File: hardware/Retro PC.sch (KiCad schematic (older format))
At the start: 0 parts

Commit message: Working on Schematic
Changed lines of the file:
@@
 $Descr A3 16535 11693
 encoding utf-8
-Sheet 1 5
+Sheet 1 6
 Title "Retro PC"
 Date "2019-10-08"
@@
 Wire Wire Line
 	10250 5450 10250 6500
+$Sheet
+S 8300 9600 1350 1250
+U 5DADBF97
+F0 "LCD" 50
+F1 "LCD.sch" 50
+$EndSheet
 $EndSCHEMATC

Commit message: Working on layout
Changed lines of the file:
@@
 Wire Wire Line
 	6500 4900 8000 4900
-$Sheet
-S 8250 6250 1600 1550
-U 5EB09E21
-F0 "Processor" 50
-F1 "Processor.sch" 50
-F2 "~RESET" I L 8250 6450 50
-F3 "PA[0..7]" O R 9850 7400 50
-F4 "CB[1..2]" I R 9850 7700 50
-F5 "PB[0..7]" I R 9850 7500 50
-F6 "TxD" O R 9850 6400 50
-F7 "RxD" I R 9850 6500 50
-F8 "RTS" O R 9850 6600 50
-F9 "CTS" I R 9850 6700 50
-F10 "ModemReady" I R 9850 6800 50
-F11 "ACIAReady" O R 9850 7300 50
-F12 "RDY" O L 8250 7500 50
-F13 "~NMI" I L 8250 7400 50
-F14 "SYNC" O L 8250 7600 50
-F15 "VPB" O L 8250 7700 50
-F16 "BE" I L 8250 7300 50
-F17 "~IRQ" I L 8250 7200 50
-$EndSheet
 Wire Wire Line
 	8250 6450 8000 6450
@@
 F4 "PA[0..7]" O R 9650 8600 50
 F5 "ACIAReady" I R 9650 8700 50
-F6 "VPB" I L 8250 9250 50
-F7 "SYNC" I L 8250 9150 50
-F8 "RDY" O L 8250 9050 50
-F9 "~NMI" O L 8250 8950 50
-F10 "BE" O L 8250 8850 50
-F11 "~IRQ" O L 8250 8750 50
+F6 "~NMI" O L 8250 8950 50
+F7 "~IRQ" O L 8250 8750 50
+F8 "R~W" I R 9650 9150 50
+F9 "A[15..0]" I R 9650 8950 50
+F10 "D[7..0]" B R 9650 9050 50
+F11 "1MHz" I R 9650 9250 50
+F12 "~RESET" O L 8250 8350 50
 $EndSheet
 Wire Bus Line
@@
 Wire Wire Line
 	9650 8700 10500 8700
-Wire Wire Line
-	10500 8700 10500 7300
-Wire Wire Line
-	10500 7300 9850 7300
 Text Notes 3550 2350 0    100  ~ 0
 VIA 1
@@
 24K
 Wire Wire Line
-	8250 9250 7550 9250
-Wire Wire Line
-	7550 9250 7550 7700
-Wire Wire Line
-	7550 7700 8250 7700
-Wire Wire Line
-	8250 9150 7650 9150
-Wire Wire Line
-	7650 9150 7650 7600
-Wire Wire Line
-	7650 7600 8250 7600
-Wire Wire Line
-	8250 7500 7750 7500
-Wire Wire Line
-	7750 7500 7750 9050
-Wire Wire Line
-	7750 9050 8250 9050
-Wire Wire Line
-	8250 8950 7850 8950
-Wire Wire Line
-	7850 8950 7850 7400
-Wire Wire Line
-	7850 7400 8250 7400
-Wire Wire Line
-	8250 7300 7950 7300
-Wire Wire Line
-	7950 7300 7950 8850
-Wire Wire Line
-	7950 8850 8250 8850
-Wire Wire Line
-	8250 8750 8050 8750
-Wire Wire Line
-	8050 8750 8050 7200
-Wire Wire Line
-	8050 7200 8250 7200
+	8250 8950 7800 8950
+Wire Wire Line
+	7800 8950 7800 7400
+Wire Wire Line
+	7800 7400 8250 7400
+Wire Wire Line
+	8250 8750 7900 8750
+Wire Wire Line
+	7900 7200 8250 7200
 Wire Wire Line
 	10250 5450 10250 6500
@@
 F1 "LCD.sch" 50
 $EndSheet
+$Sheet
+S 8250 6250 1600 1550
+U 5EB09E21
+F0 "Processor" 50
+F1 "Processor.sch" 50
+F2 "~RESET" I L 8250 6450 50
+F3 "PA[0..7]" O R 9850 7400 50
+F4 "CB[1..2]" I R 9850 7700 50
+F5 "PB[0..7]" I R 9850 7500 50
+F6 "TxD" O R 9850 6400 50
+F7 "RxD" I R 9850 6500 50
+F8 "RTS" O R 9850 6600 50
+F9 "CTS" I R 9850 6700 50
+F10 "ModemReady" I R 9850 6800 50
+F11 "ACIAReady" O R 9850 7600 50
+F12 "~NMI" I L 8250 7400 50
+F13 "~IRQ" I L 8250 7200 50
+F14 "LCD[0..7]" I L 8250 6700 50
+F15 "R~W" O R 9850 7150 50
+F16 "A[15..0]" O R 9850 6950 50
+F17 "D[7..0]" B R 9850 7050 50
+F18 "1MHz" O R 9850 7250 50
+$EndSheet
+Wire Bus Line
+	9850 6950 10900 6950
+Wire Bus Line
+	10900 6950 10900 8950
+Wire Bus Line
+	10900 8950 9650 8950
+Wire Bus Line
+	10800 7050 10800 9050
+Wire Bus Line
+	10800 9050 9650 9050
+Wire Bus Line
+	9850 7050 10800 7050
+Wire Wire Line
+	9650 9150 10700 9150
+Wire Wire Line
+	10700 7150 9850 7150
+Wire Wire Line
+	10700 9150 10700 7150
+Wire Wire Line
+	10500 8700 10500 7600
+Wire Wire Line
+	10500 7600 9850 7600
+Wire Wire Line
+	9850 7250 10600 7250
+Wire Wire Line
+	10600 7250 10600 9250
+Wire Wire Line
+	10600 9250 9650 9250
+Wire Wire Line
+	7900 8750 7900 7200
+Connection ~ 8000 6450
+Wire Wire Line
+	8250 8350 8000 8350
+Wire Wire Line
+	8000 6450 8000 8350
 $EndSCHEMATC

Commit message: Working on layout
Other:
- note added: "VIA 2"
- note removed: "VIA 2 (Not available)"
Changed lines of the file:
@@
 VIA 1
 Text Notes 3550 2600 0    100  ~ 0
-VIA 2 (Not available)
+VIA 2
 Text Notes 900  2600 0    100  ~ 0
 $8400 - $87FF

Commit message: Working on layout
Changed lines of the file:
@@
 F2 "~RESET" O R 6500 4900 50
-$EndSheet
-$Sheet
-S 8200 4700 1650 1250
-U 5E9064F2
-F0 "USB" 50
-F1 "USB.sch" 50
-F2 "~RESET" I L 8200 4900 50
-F3 "TxD" I R 9850 5450 50
-F4 "RxD" I R 9850 5550 50
-F5 "CTS" I R 9850 5650 50
-F6 "RTS" O R 9850 5750 50
-F7 "ModemReady" O R 9850 5850 50
 $EndSheet
 Wire Bus Line
@@
 F3 "PB[0..7]" O R 9650 8500 50
 F4 "PA[0..7]" O R 9650 8600 50
-F5 "ACIAReady" I R 9650 8700 50
-F6 "~NMI" O L 8250 8950 50
-F7 "~IRQ" O L 8250 8750 50
-F8 "R~W" I R 9650 9150 50
-F9 "A[15..0]" I R 9650 8950 50
-F10 "D[7..0]" B R 9650 9050 50
-F11 "1MHz" I R 9650 9250 50
-F12 "~RESET" O L 8250 8350 50
+F5 "~NMI" O L 8250 8950 50
+F6 "~IRQ" O L 8250 8750 50
+F7 "R~W" I R 9650 9150 50
+F8 "A[15..0]" I R 9650 8950 50
+F9 "D[7..0]" B R 9650 9050 50
+F10 "~RESET" O L 8250 8350 50
+F11 "Clock" I R 9650 9250 50
 $EndSheet
 Wire Bus Line
 	9650 8500 10250 8500
 Wire Bus Line
-	10250 8500 10250 7500
+	10250 8500 10250 7600
 Wire Bus Line
 	9650 8600 10350 8600
 Wire Bus Line
-	10350 8600 10350 7400
+	10350 8600 10350 7500
 Text Notes 900  1850 0    100  ~ 0
 $0000 - $FFFF\n
@@
 Wire Notes Line width 18 style solid
 	750  1150 750  3700
-Wire Bus Line
-	9850 7400 10350 7400
-Wire Bus Line
-	9850 7500 10250 7500
 Wire Wire Line
 	9850 5450 10250 5450
@@
 	9850 5650 10150 5650
 Wire Wire Line
-	10150 5650 10150 6600
+	10150 5650 10150 6550
 Wire Wire Line
-	10150 6600 9850 6600
-Wire Wire Line
-	9850 6700 10100 6700
-Wire Wire Line
-	10100 6700 10100 5750
+	10150 6550 9850 6550
 Wire Wire Line
 	10100 5750 9850 5750
@@
 	9850 5850 10050 5850
 Wire Wire Line
-	10050 5850 10050 6800
+	10050 5850 10050 6750
 Wire Wire Line
-	10050 6800 9850 6800
+	10050 6750 9850 6750
 Wire Wire Line
-	9850 6400 10200 6400
+	9850 6350 10200 6350
 Wire Wire Line
-	10200 6400 10200 5550
+	10200 6350 10200 5550
 Wire Wire Line
-	9850 6500 10250 6500
-Wire Wire Line
-	9650 8700 10500 8700
+	9850 6450 10250 6450
 Text Notes 3550 2350 0    100  ~ 0
 VIA 1
@@
 	8250 8950 7800 8950
 Wire Wire Line
-	7800 8950 7800 7400
-Wire Wire Line
-	7800 7400 8250 7400
-Wire Wire Line
 	8250 8750 7900 8750
 Wire Wire Line
-	7900 7200 8250 7200
+	7900 7650 8250 7650
 Wire Wire Line
-	10250 5450 10250 6500
+	10250 5450 10250 6450
 $Sheet
-S 8300 9600 1350 1250
+S 5150 6350 1350 1250
 U 5DADBF97
-F0 "LCD" 50
-F1 "LCD.sch" 50
+F0 "LCD / PS2" 50
+F1 "LCD_PS2.sch" 50
+F2 "LCD[0..10]" B R 6500 6700 50
+F3 "PS2[0..1]" B R 6500 6800 50
 $EndSheet
 $Sheet
@@
 F1 "Processor.sch" 50
 F2 "~RESET" I L 8250 6450 50
-F3 "PA[0..7]" O R 9850 7400 50
+F3 "PA[0..7]" O R 9850 7500 50
 F4 "CB[1..2]" I R 9850 7700 50
-F5 "PB[0..7]" I R 9850 7500 50
-F6 "TxD" O R 9850 6400 50
-F7 "RxD" I R 9850 6500 50
-F8 "RTS" O R 9850 6600 50
-F9 "CTS" I R 9850 6700 50
-F10 "ModemReady" I R 9850 6800 50
-F11 "ACIAReady" O R 9850 7600 50
-F12 "~NMI" I L 8250 7400 50
-F13 "~IRQ" I L 8250 7200 50
-F14 "LCD[0..7]" I L 8250 6700 50
-F15 "R~W" O R 9850 7150 50
-F16 "A[15..0]" O R 9850 6950 50
-F17 "D[7..0]" B R 9850 7050 50
-F18 "1MHz" O R 9850 7250 50
+F5 "PB[0..7]" I R 9850 7600 50
+F6 "TxD" O R 9850 6350 50
+F7 "RxD" I R 9850 6450 50
+F8 "RTS" O R 9850 6550 50
+F9 "CTS" I R 9850 6650 50
+F10 "~NMI" I L 8250 7750 50
+F11 "~IRQ" I L 8250 7650 50
+F12 "R~W" O R 9850 7250 50
+F13 "A[15..0]" O R 9850 7050 50
+F14 "D[7..0]" B R 9850 7150 50
+F15 "RDY" O L 8250 7100 50
+F16 "SYNC" O L 8250 7000 50
+F17 "VPB" O L 8250 6950 50
+F18 "BE" I L 8250 7450 50
+F19 "LCD[0..10]" B L 8250 6700 50
+F20 "PS2[0..1]" B L 8250 6800 50
+F21 "~ModemReady" I R 9850 6750 50
+F22 "~ReceiverReady" O R 9850 6850 50
+F23 "Clock" O R 9850 7350 50
+F24 "~Carrier" I R 9850 6950 50
 $EndSheet
-Wire Bus Line
-	9850 6950 10900 6950
-Wire Bus Line
-	10900 6950 10900 8950
 Wire Bus Line
 	10900 8950 9650 8950
 Wire Bus Line
-	10800 7050 10800 9050
-Wire Bus Line
 	10800 9050 9650 9050
 Wire Bus Line
-	9850 7050 10800 7050
+	9850 7150 10800 7150
 Wire Wire Line
 	9650 9150 10700 9150
 Wire Wire Line
-	10700 7150 9850 7150
+	10700 9150 10700 7250
 Wire Wire Line
-	10700 9150 10700 7150
-Wire Wire Line
-	10500 8700 10500 7600
-Wire Wire Line
-	10500 7600 9850 7600
-Wire Wire Line
-	9850 7250 10600 7250
-Wire Wire Line
-	10600 7250 10600 9250
+	9850 7350 10600 7350
 Wire Wire Line
 	10600 9250 9650 9250
 Wire Wire Line
-	7900 8750 7900 7200
+	7900 8750 7900 7650
 Connection ~ 8000 6450
 Wire Wire Line
@@
 Wire Wire Line
 	8000 6450 8000 8350
+Wire Bus Line
+	6500 6800 8250 6800
+Wire Bus Line
+	8250 6700 6500 6700
+Wire Wire Line
+	10100 6650 10100 5750
+Wire Wire Line
+	9850 6650 10100 6650
+$Sheet
+S 8200 4700 1650 1250
+U 5E9064F2
+F0 "USB" 50
+F1 "USB.sch" 50
+F2 "~RESET" I L 8200 4900 50
+F3 "TxD" I R 9850 5450 50
+F4 "RxD" I R 9850 5550 50
+F5 "CTS" I R 9850 5650 50
+F6 "RTS" O R 9850 5750 50
+F7 "~ModemReady" O R 9850 5850 50
+$EndSheet
+Wire Bus Line
+	9850 7600 10250 7600
+Wire Bus Line
+	9850 7500 10350 7500
+Wire Wire Line
+	10600 7350 10600 9250
+Wire Bus Line
+	10800 7150 10800 9050
+Wire Bus Line
+	10900 7050 10900 8950
+Wire Wire Line
+	9850 7250 10700 7250
+Wire Bus Line
+	9850 7050 10900 7050
+Wire Wire Line
+	7800 7750 8250 7750
+Wire Wire Line
+	7800 7750 7800 8950
 $EndSCHEMATC

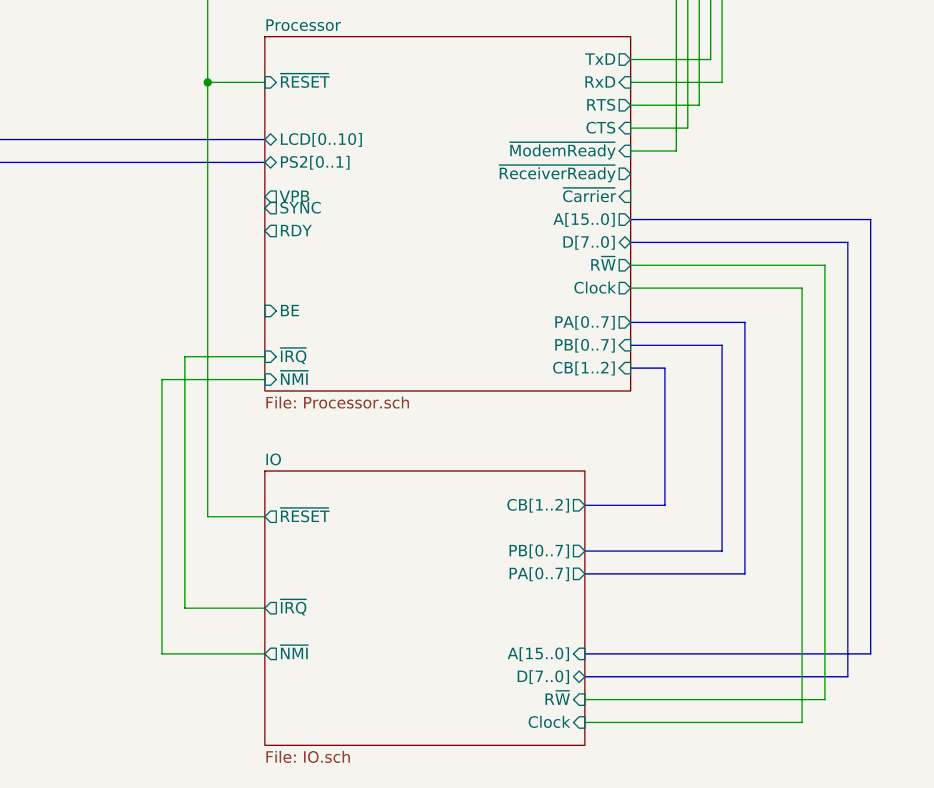
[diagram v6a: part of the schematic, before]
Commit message: Finalize schematic and layout. Add switch for carrier detect
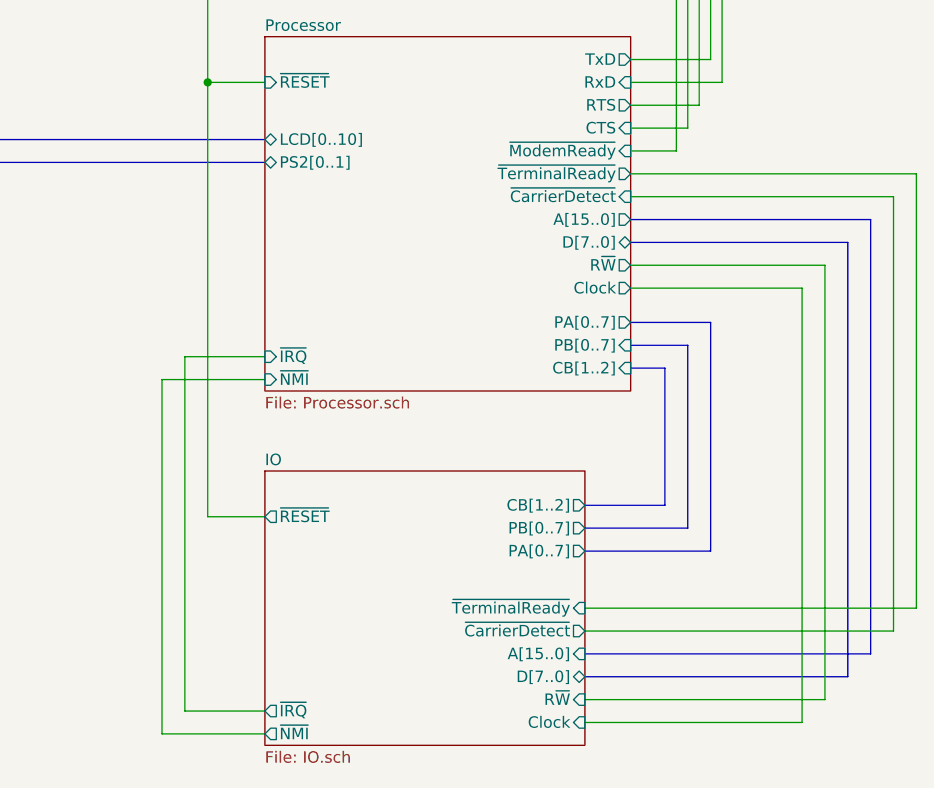
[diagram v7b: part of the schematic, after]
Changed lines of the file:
@@
 Date "2019-10-08"
 Rev "1.0"
-Comp ""
+Comp "https://www.kampis-elektroecke.de"
 Comment1 "Author: Daniel Kampert"
 Comment2 ""
@@
 F1 "IO.sch" 50
 F2 "CB[1..2]" O R 9650 8300 50
-F3 "PB[0..7]" O R 9650 8500 50
-F4 "PA[0..7]" O R 9650 8600 50
-F5 "~NMI" O L 8250 8950 50
-F6 "~IRQ" O L 8250 8750 50
+F3 "PB[0..7]" O R 9650 8400 50
+F4 "PA[0..7]" O R 9650 8500 50
+F5 "~NMI" O L 8250 9300 50
+F6 "~IRQ" O L 8250 9200 50
 F7 "R~W" I R 9650 9150 50
 F8 "A[15..0]" I R 9650 8950 50
@@
 F10 "~RESET" O L 8250 8350 50
 F11 "Clock" I R 9650 9250 50
-$EndSheet
-Wire Bus Line
-	9650 8500 10250 8500
-Wire Bus Line
-	10250 8500 10250 7600
-Wire Bus Line
-	9650 8600 10350 8600
-Wire Bus Line
-	10350 8600 10350 7500
+F12 "~TerminalReady" I R 9650 8750 50
+F13 "~CarrierDetect" O R 9650 8850 50
+$EndSheet
 Text Notes 900  1850 0    100  ~ 0
 $0000 - $FFFF\n
@@
 Text Notes 2650 3100 0    100  ~ 0
 24K
-Wire Wire Line
-	8250 8950 7800 8950
-Wire Wire Line
-	8250 8750 7900 8750
 Wire Wire Line
 	7900 7650 8250 7650
@@
 F13 "A[15..0]" O R 9850 7050 50
 F14 "D[7..0]" B R 9850 7150 50
-F15 "RDY" O L 8250 7100 50
-F16 "SYNC" O L 8250 7000 50
-F17 "VPB" O L 8250 6950 50
-F18 "BE" I L 8250 7450 50
-F19 "LCD[0..10]" B L 8250 6700 50
-F20 "PS2[0..1]" B L 8250 6800 50
-F21 "~ModemReady" I R 9850 6750 50
-F22 "~ReceiverReady" O R 9850 6850 50
-F23 "Clock" O R 9850 7350 50
-F24 "~Carrier" I R 9850 6950 50
+F15 "LCD[0..10]" B L 8250 6700 50
+F16 "PS2[0..1]" B L 8250 6800 50
+F17 "~ModemReady" I R 9850 6750 50
+F18 "Clock" O R 9850 7350 50
+F19 "~TerminalReady" O R 9850 6850 50
+F20 "~CarrierDetect" I R 9850 6950 50
 $EndSheet
 Wire Bus Line
@@
 Wire Wire Line
 	10600 9250 9650 9250
-Wire Wire Line
-	7900 8750 7900 7650
 Connection ~ 8000 6450
 Wire Wire Line
@@
 $EndSheet
 Wire Bus Line
-	9850 7600 10250 7600
-Wire Bus Line
-	9850 7500 10350 7500
+	9850 7600 10100 7600
+Wire Bus Line
+	9850 7500 10200 7500
 Wire Wire Line
 	10600 7350 10600 9250
@@
 Wire Wire Line
 	7800 7750 8250 7750
-Wire Wire Line
-	7800 7750 7800 8950
+Wire Bus Line
+	9650 8400 10100 8400
+Wire Bus Line
+	10100 8400 10100 7600
+Wire Bus Line
+	9650 8500 10200 8500
+Wire Bus Line
+	10200 8500 10200 7500
+Wire Wire Line
+	11100 6850 11100 8750
+Wire Wire Line
+	9850 6850 11100 6850
+Wire Wire Line
+	9650 8750 11100 8750
+Wire Wire Line
+	9650 8850 11000 8850
+Wire Wire Line
+	11000 8850 11000 6950
+Wire Wire Line
+	11000 6950 9850 6950
+Wire Wire Line
+	8250 9200 7900 9200
+Wire Wire Line
+	8250 9300 7800 9300
+Wire Wire Line
+	7800 7750 7800 9300
+Wire Wire Line
+	7900 7650 7900 9200
 $EndSCHEMATC
